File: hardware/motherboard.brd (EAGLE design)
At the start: 109 x 84 mm, 46 parts, among them IC1 7805T, Q1 16MHz, U1 ATMEGA328P-PU, U2 L293NE

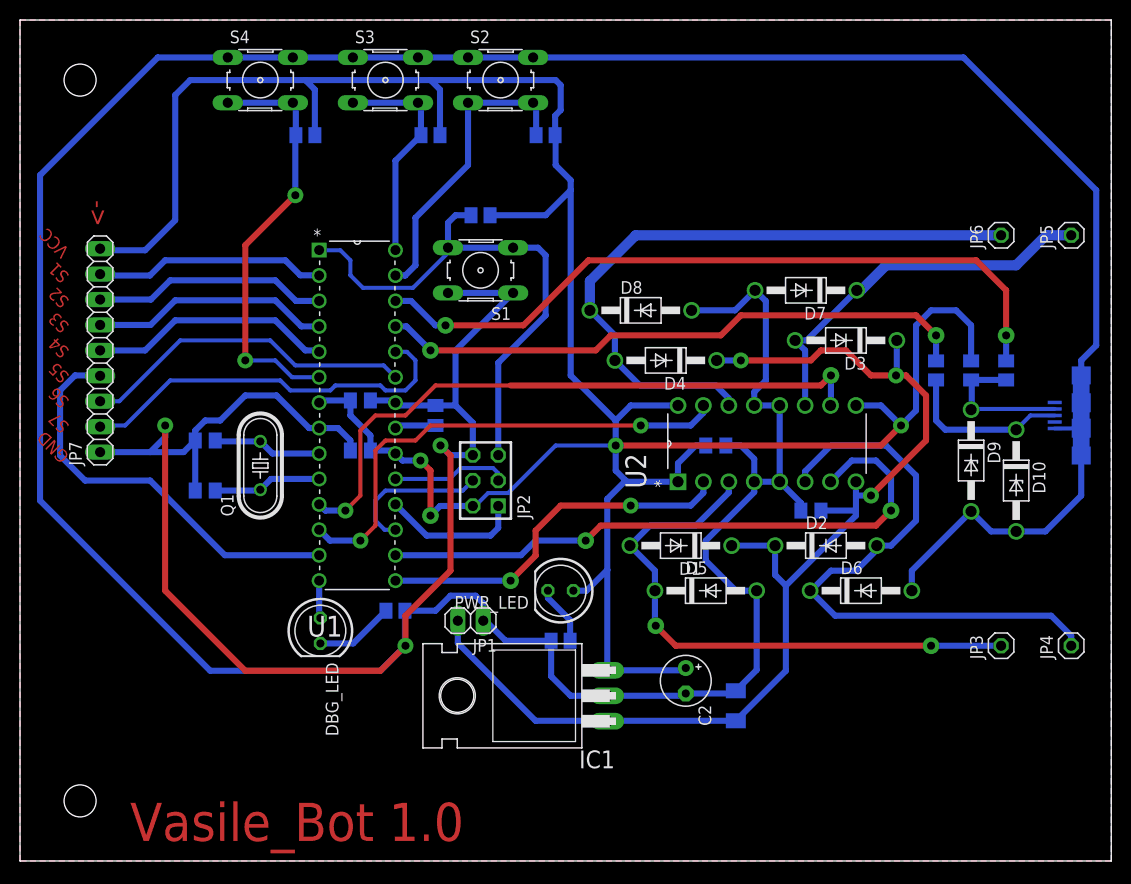
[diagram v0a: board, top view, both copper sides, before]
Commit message: Fixed motors space. Added motors halls.
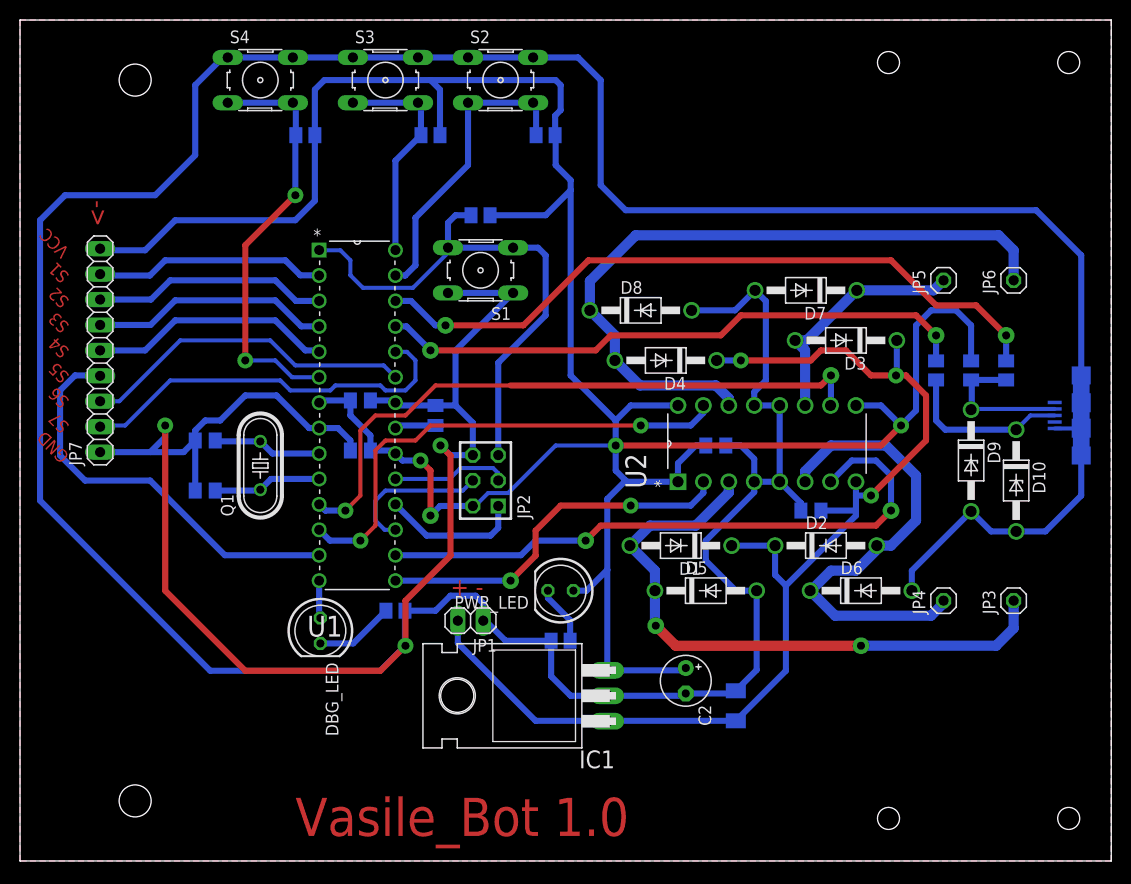
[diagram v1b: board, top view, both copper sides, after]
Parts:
- moved JP4 13.5 mm to (92.2, 26.0)
- moved JP5 13.5 mm to (92.2, 58.0)
- moved JP3 4.67 mm to (99.2, 26.0)
- moved JP6 4.67 mm to (99.2, 58.0)
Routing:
- net N$6: track 38.8 -> 24.2 mm
- net N$5: track 61.6 -> 47.8 mm
- net VCC: track 270.9 -> 264.2 mm
- net N$7: track 65.6 -> 70.5 mm
- net N$4: track 57.6 -> 62.3 mm
- net D-: track 73.0 -> 70.4 mm
- net GND: track 508.2 -> 509.9 mm
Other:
- board text added: "+"
- board text added: "-"

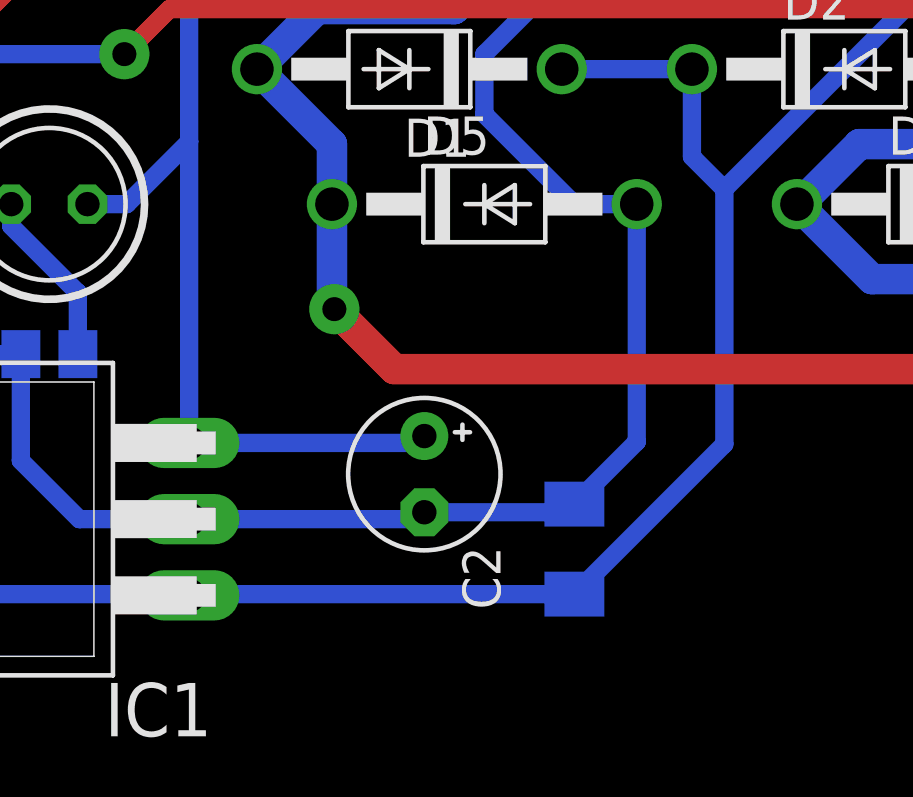
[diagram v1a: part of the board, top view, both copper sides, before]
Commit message: Added partlists for boards.
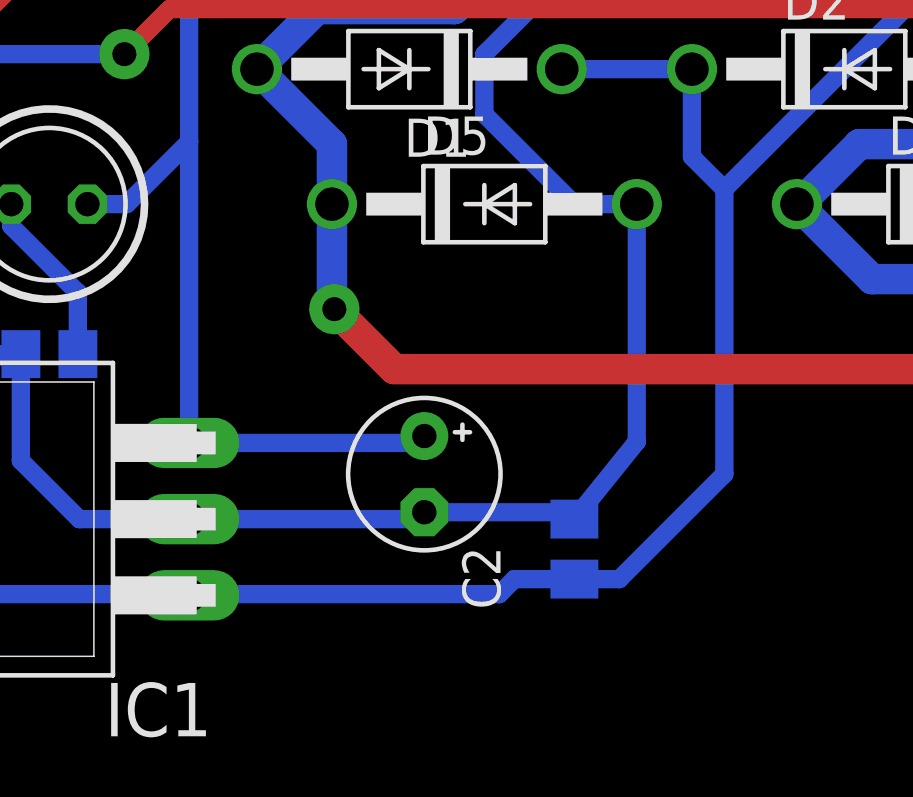
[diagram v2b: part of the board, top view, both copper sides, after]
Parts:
- C1: device resistor:C1206K -> resistor:C0805K
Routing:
- net VCC/2: track 114.9 -> 115.5 mm
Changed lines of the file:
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@@
 <?xml version="1.0" encoding="utf-8"?>
 <!DOCTYPE eagle SYSTEM "eagle.dtd">
-<eagle version="7.5.0">
+<eagle version="7.6.0">
 <drawing>
 <settings>
@@
 </autorouter>
 <elements>
-<element name="C1" library="resistor" package="C1206K" value="330n" x="71.5" y="15.5" rot="MR90"/>
+<element name="C1" library="resistor" package="C0805K" value="330n" x="71.5" y="15.5" rot="MR90"/>
 <element name="C2" library="resistor" package="E2,5-5" value="100u" x="66.5" y="18" rot="R270"/>
 <element name="C3" library="resistor" package="C0805K" value="22p" x="18.5" y="42" rot="MR180"/>
@@
 <contactref element="U2" pad="8"/>
 <contactref element="C8" pad="2"/>
-<wire x1="58.66" y1="13.96" x2="58.7" y2="14" width="0.6096" layer="16"/>
-<wire x1="58.7" y1="14" x2="71.5" y2="14" width="0.6096" layer="16"/>
 <wire x1="58.62" y1="14" x2="58.66" y2="13.96" width="0.6096" layer="16"/>
-<wire x1="76.5" y1="19" x2="76.5" y2="27.5" width="0.6096" layer="16"/>
+<wire x1="76.5" y1="18" x2="76.5" y2="27.5" width="0.6096" layer="16"/>
 <wire x1="76.5" y1="27.5" x2="83.5" y2="34.5" width="0.6096" layer="16"/>
 <wire x1="83.5" y1="34.5" x2="83.5" y2="35" width="0.6096" layer="16"/>
@@
 <wire x1="83.5" y1="36.5" x2="83.5" y2="37.88" width="0.6096" layer="16"/>
 <wire x1="80" y1="35" x2="83.5" y2="35" width="0.6096" layer="16"/>
-<wire x1="71.5" y1="14" x2="76.5" y2="19" width="0.6096" layer="16"/>
 <wire x1="58.62" y1="14" x2="51.5" y2="14" width="0.6096" layer="16"/>
 <wire x1="43.73" y1="24" x2="43.73" y2="21.77" width="0.6096" layer="16"/>
@@
 <via x="85" y="36.5" extent="1-16" drill="0.8" diameter="1.6"/>
 <wire x1="85" y1="36.5" x2="83.5" y2="36.5" width="0.6096" layer="16"/>
+<wire x1="76.5" y1="18" x2="73" y2="14.5" width="0.6096" layer="16"/>
+<wire x1="73" y1="14.5" x2="71.5" y2="14.5" width="0.6096" layer="16"/>
+<wire x1="71.5" y1="14.5" x2="69.5" y2="14.5" width="0.6096" layer="16"/>
+<wire x1="69.5" y1="14.5" x2="69" y2="14" width="0.6096" layer="16"/>
+<wire x1="69" y1="14" x2="58.7" y2="14" width="0.6096" layer="16"/>
+<wire x1="58.7" y1="14" x2="58.66" y2="13.96" width="0.6096" layer="16"/>
 </signal>
 <signal name="GND">
@@
 <wire x1="89.08" y1="27" x2="89.08" y2="29" width="0.6096" layer="16"/>
 <wire x1="89.08" y1="29" x2="95" y2="34.92" width="0.6096" layer="16"/>
-<wire x1="71.23" y1="16.73" x2="71.5" y2="17" width="0.6096" layer="16"/>
-<wire x1="71.5" y1="17" x2="73.58" y2="19.08" width="0.6096" layer="16"/>
+<wire x1="71.23" y1="16.73" x2="71.5" y2="16.5" width="0.6096" layer="16"/>
+<wire x1="71.5" y1="16.5" x2="73.58" y2="19.08" width="0.6096" layer="16"/>
 <wire x1="49.2512" y1="56.7394" x2="43.5" y2="50.9882" width="0.6096" layer="16"/>
 <wire x1="43.5" y1="50.9882" x2="43.5" y2="45.5" width="0.6096" layer="16"/>

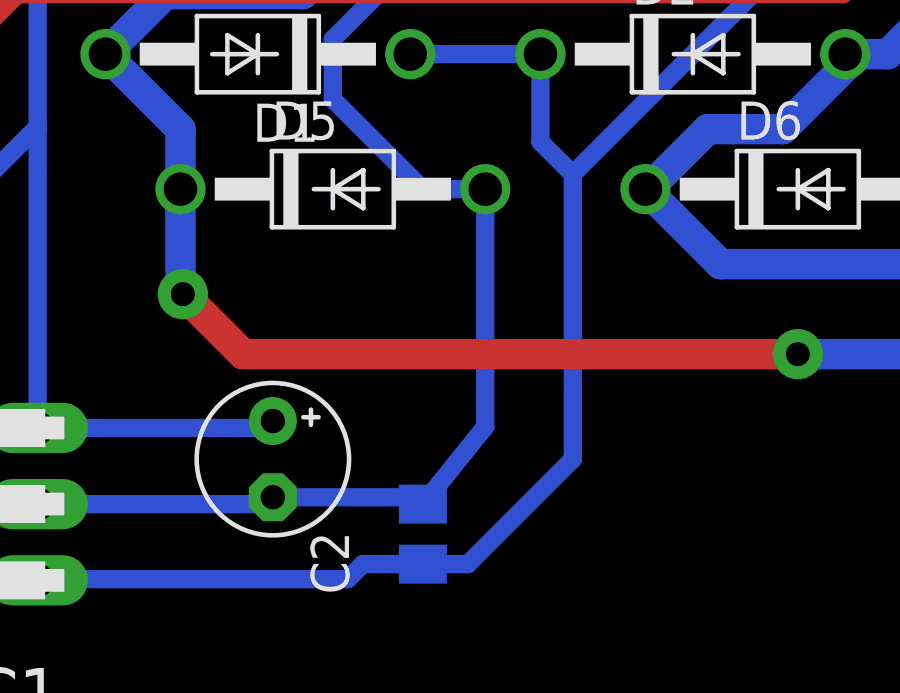
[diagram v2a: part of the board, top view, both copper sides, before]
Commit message: Beautified sensorboard and motherboard schematics. Fixed motherboard angle error.
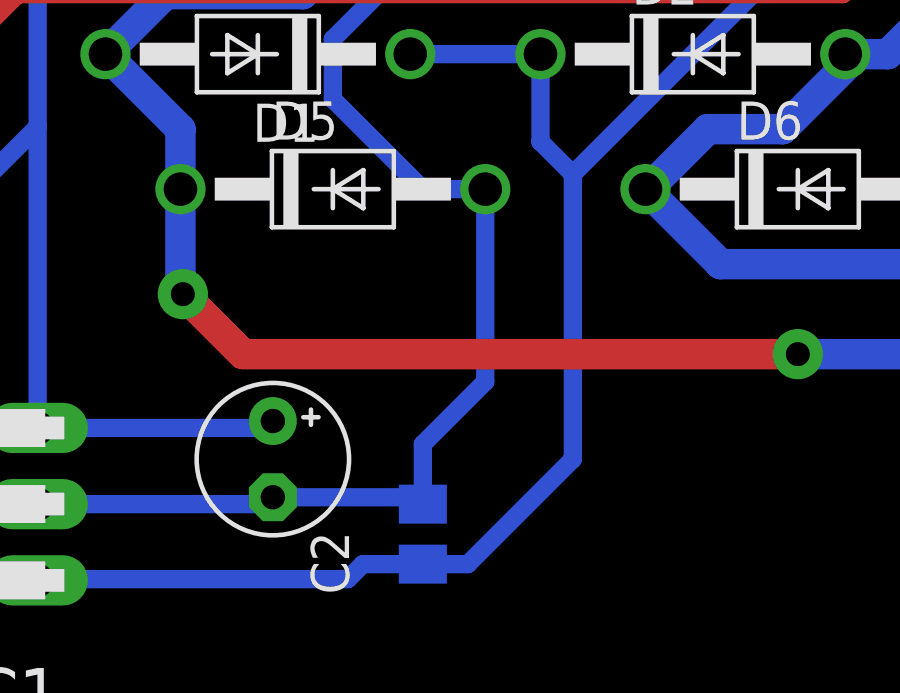
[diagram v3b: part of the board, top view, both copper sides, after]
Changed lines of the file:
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@@
 <wire x1="58.66" y1="16.5" x2="66.27" y2="16.5" width="0.6096" layer="16"/>
 <wire x1="66.27" y1="16.5" x2="66.5" y2="16.73" width="0.6096" layer="16"/>
-<wire x1="73.58" y1="27" x2="73.58" y2="19.08" width="0.6096" layer="16"/>
+<wire x1="73.58" y1="27" x2="73.58" y2="20.58" width="0.6096" layer="16"/>
 <wire x1="66.5" y1="16.73" x2="71.23" y2="16.73" width="0.6096" layer="16"/>
 <wire x1="45.23" y1="40.54" x2="45.23" y2="43.77" width="0.6096" layer="16"/>
@@
 <wire x1="89.08" y1="27" x2="89.08" y2="29" width="0.6096" layer="16"/>
 <wire x1="89.08" y1="29" x2="95" y2="34.92" width="0.6096" layer="16"/>
-<wire x1="71.23" y1="16.73" x2="71.5" y2="16.5" width="0.6096" layer="16"/>
-<wire x1="71.5" y1="16.5" x2="73.58" y2="19.08" width="0.6096" layer="16"/>
 <wire x1="49.2512" y1="56.7394" x2="43.5" y2="50.9882" width="0.6096" layer="16"/>
 <wire x1="43.5" y1="50.9882" x2="43.5" y2="45.5" width="0.6096" layer="16"/>
@@
 <wire x1="101.5" y1="65" x2="106" y2="60.5" width="0.6096" layer="16"/>
 <wire x1="106" y1="60.5" x2="106" y2="48.5" width="0.6096" layer="16"/>
+<wire x1="73.58" y1="20.58" x2="71.5" y2="18.5" width="0.6096" layer="16"/>
+<wire x1="71.5" y1="18.5" x2="71.5" y2="16.5" width="0.6096" layer="16"/>
 </signal>
 <signal name="VCC">
